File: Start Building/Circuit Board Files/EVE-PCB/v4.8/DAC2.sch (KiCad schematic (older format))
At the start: 26 parts, among them Q10 DMN6140LQ-7, Q11 DMN6140LQ-7, Q4 ULN2803ADWR, Q5 ULN2803ADWR, U8 MCP23017-E/SO

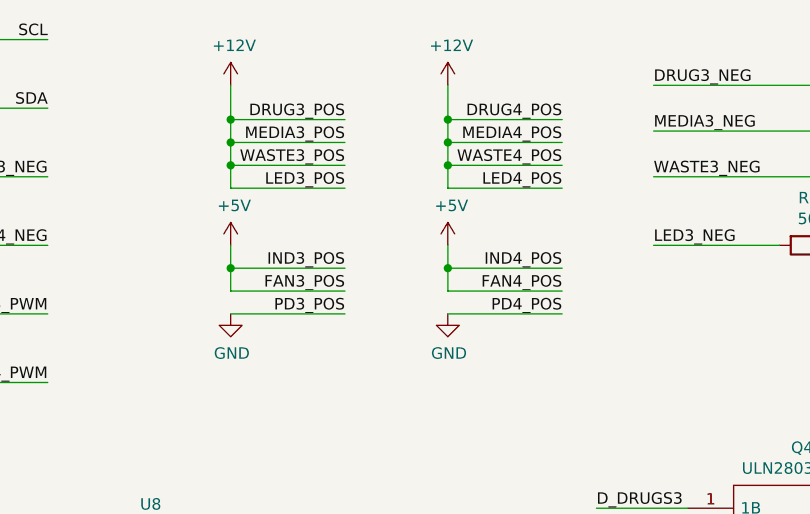
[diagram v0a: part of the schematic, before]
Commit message: Bump PCB version to 4.81
- Fixed voltages for fan and LED
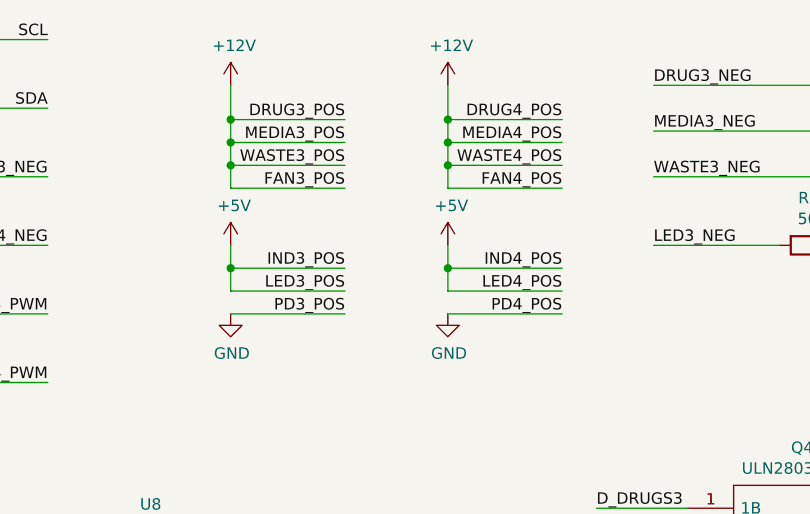
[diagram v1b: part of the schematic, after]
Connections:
- net +12V: now also L3.10, L4.10; no longer L3.11, L4.11
- net +5V: now also L3.11, L4.11; no longer L3.10, L4.10
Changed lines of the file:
@@
 $Descr A4 11693 8268
 encoding utf-8
-Sheet 3 3
+Sheet 2 3
 Title ""
 Date ""
@@
 WASTE3_POS
 Text Label 3250 1400 2    50   ~ 0
-LED3_POS
+FAN3_POS
 $Comp
 L EVE-PCB-V4-rescue:+12V-power-EVE-PCB-rescue #PWR?
@@
 WASTE4_POS
 Text Label 4200 1400 2    50   ~ 0
-LED4_POS
+FAN4_POS
 $Comp
 L EVE-PCB-V4-rescue:+12V-power-EVE-PCB-rescue #PWR?
@@
 	4200 1850 3700 1850
 Text Label 4200 1850 2    50   ~ 0
-FAN4_POS
+LED4_POS
 Text Label 3250 1850 2    50   ~ 0
-FAN3_POS
+LED3_POS
 Wire Wire Line
 	3250 1850 2750 1850

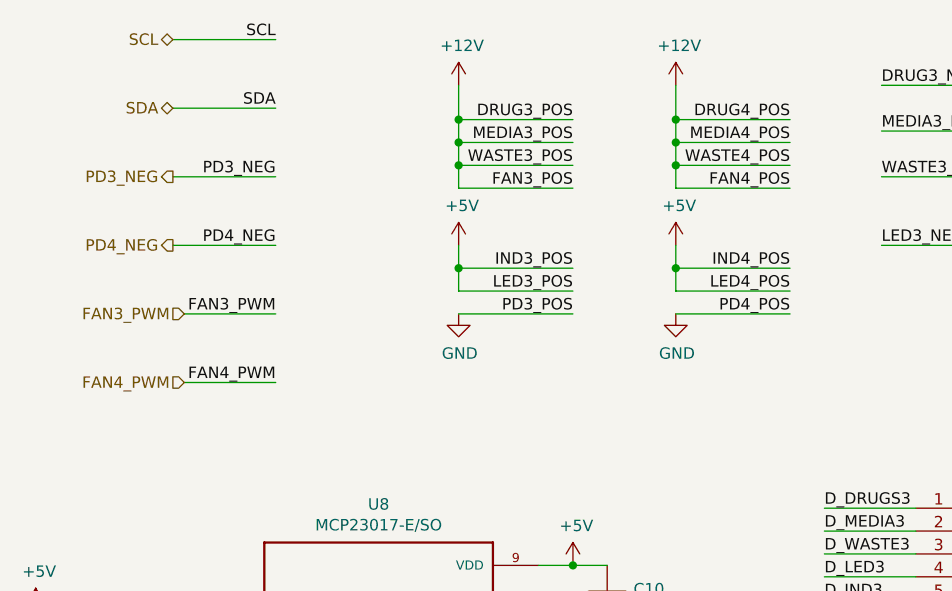
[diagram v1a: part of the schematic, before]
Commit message: Bump PCB to version 4.82
- Update schematic to use V_ref as PD positive terminal.
- Update PCB to allow for this change.
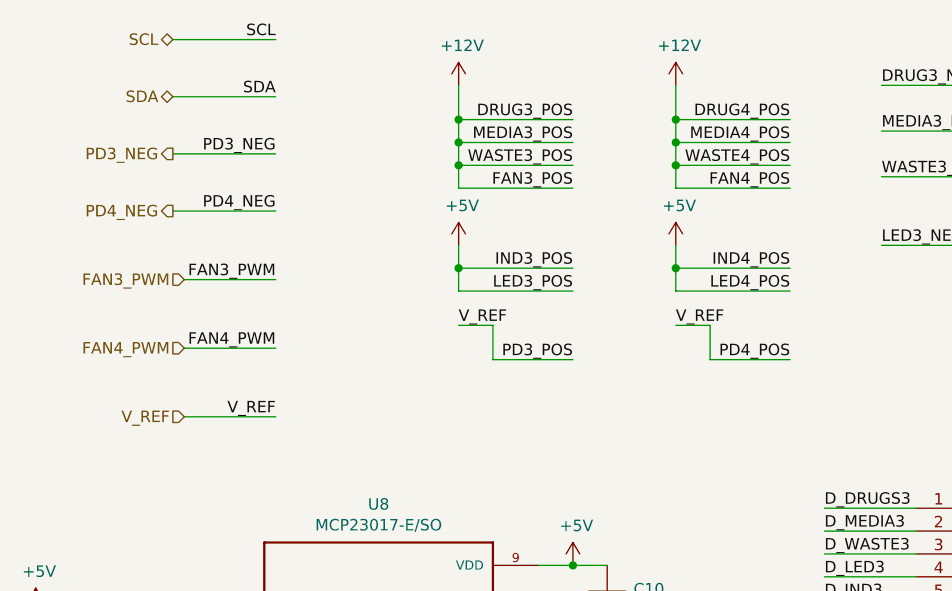
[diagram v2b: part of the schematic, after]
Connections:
- net GND: no longer L3.12, L4.12
- new net V_REF: L3.12, L4.12
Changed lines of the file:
@@
 Text HLabel 1500 750  0    50   BiDi ~ 0
 SCL
-Text HLabel 1500 1050 0    50   BiDi ~ 0
+Text HLabel 1500 1000 0    50   BiDi ~ 0
 SDA
 Text Label 1950 750  2    50   ~ 0
 SCL
-Text Label 1950 1050 2    50   ~ 0
+Text Label 1950 1000 2    50   ~ 0
 SDA
 Wire Wire Line
@@
 	1500 750  1950 750
 Wire Wire Line
-	1500 1050 1950 1050
+	1500 1000 1950 1000
 NoConn ~ 3100 4550
 NoConn ~ 1700 4650
@@
 Wire Wire Line
 	7300 5150 7800 5150
-Text Label 3250 1950 2    50   ~ 0
-PD3_POS
-$Comp
-L EVE-PCB-V4-rescue:GND-power-EVE-PCB-rescue #PWR?
-U 1 1 5CD887EE
-P 2750 1950
-AR Path="/5CA7DFAE/5CD887EE" Ref="#PWR?"  Part="1"
-AR Path="/5CA80A88/5CD887EE" Ref="#PWR054"  Part="1"
-F 0 "#PWR054" H 2750 1700 50  0001 C CNN
-F 1 "GND" H 2755 1777 50  0000 C CNN
-F 2 "" H 2750 1950 50  0001 C CNN
-F 3 "" H 2750 1950 50  0001 C CNN
-	1    2750 1950
-	1    0    0    -1
-$EndComp
-Wire Wire Line
-	2750 1950 3250 1950
-Text Label 4200 1950 2    50   ~ 0
-PD4_POS
-$Comp
-L EVE-PCB-V4-rescue:GND-power-EVE-PCB-rescue #PWR?
-U 1 1 5CD887F6
-P 3700 1950
-AR Path="/5CA7DFAE/5CD887F6" Ref="#PWR?"  Part="1"
-AR Path="/5CA80A88/5CD887F6" Ref="#PWR059"  Part="1"
-F 0 "#PWR059" H 3700 1700 50  0001 C CNN
-F 1 "GND" H 3705 1777 50  0000 C CNN
-F 2 "" H 3700 1950 50  0001 C CNN
-F 3 "" H 3700 1950 50  0001 C CNN
-	1    3700 1950
-	1    0    0    -1
-$EndComp
-Wire Wire Line
-	3700 1950 4200 1950
-Text Label 1950 1650 2    50   ~ 0
+Text Label 1950 1500 2    50   ~ 0
 PD4_NEG
-Text Label 1950 1350 2    50   ~ 0
+Text Label 1950 1250 2    50   ~ 0
 PD3_NEG
-Text HLabel 1500 1350 0    50   Output ~ 0
+Text HLabel 1500 1250 0    50   Output ~ 0
 PD3_NEG
-Text HLabel 1500 1650 0    50   Output ~ 0
+Text HLabel 1500 1500 0    50   Output ~ 0
 PD4_NEG
 Wire Wire Line
-	1500 1350 1950 1350
-Wire Wire Line
-	1500 1650 1950 1650
+	1500 1250 1950 1250
+Wire Wire Line
+	1500 1500 1950 1500
 Text Label 1300 4350 0    50   ~ 0
 D_IND4
@@
 NoConn ~ 5750 3400
 NoConn ~ 5750 3300
-Text Label 1950 1950 2    50   ~ 0
+Text Label 1950 1800 2    50   ~ 0
 FAN3_PWM
-Text Label 1950 2250 2    50   ~ 0
+Text Label 1950 2100 2    50   ~ 0
 FAN4_PWM
 Wire Wire Line
-	1950 1950 1550 1950
-Wire Wire Line
-	1950 2250 1550 2250
-Text HLabel 1550 1950 0    50   Input ~ 0
+	1950 1800 1550 1800
+Wire Wire Line
+	1950 2100 1550 2100
+Text HLabel 1550 1800 0    50   Input ~ 0
 FAN3_PWM
-Text HLabel 1550 2250 0    50   Input ~ 0
+Text HLabel 1550 2100 0    50   Input ~ 0
 FAN4_PWM
 Wire Wire Line
@@
 	1    0    0    -1
 $EndComp
+Text HLabel 1550 2400 0    50   Input ~ 0
+V_REF
+Text Label 1950 2400 2    50   ~ 0
+V_REF
+Wire Wire Line
+	1950 2400 1550 2400
+Text Label 3250 2150 2    50   ~ 0
+PD3_POS
+Text Label 4200 2150 2    50   ~ 0
+PD4_POS
+Text Label 2750 2000 0    50   ~ 0
+V_REF
+Text Label 3700 2000 0    50   ~ 0
+V_REF
+Wire Wire Line
+	3700 2000 3850 2000
+Wire Wire Line
+	3850 2000 3850 2150
+Wire Wire Line
+	3850 2150 4200 2150
+Wire Wire Line
+	2750 2000 2900 2000
+Wire Wire Line
+	2900 2000 2900 2150
+Wire Wire Line
+	2900 2150 3250 2150
 $EndSCHEMATC
